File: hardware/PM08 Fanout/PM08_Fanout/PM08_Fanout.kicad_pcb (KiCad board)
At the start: 2 copper layers, 1 part

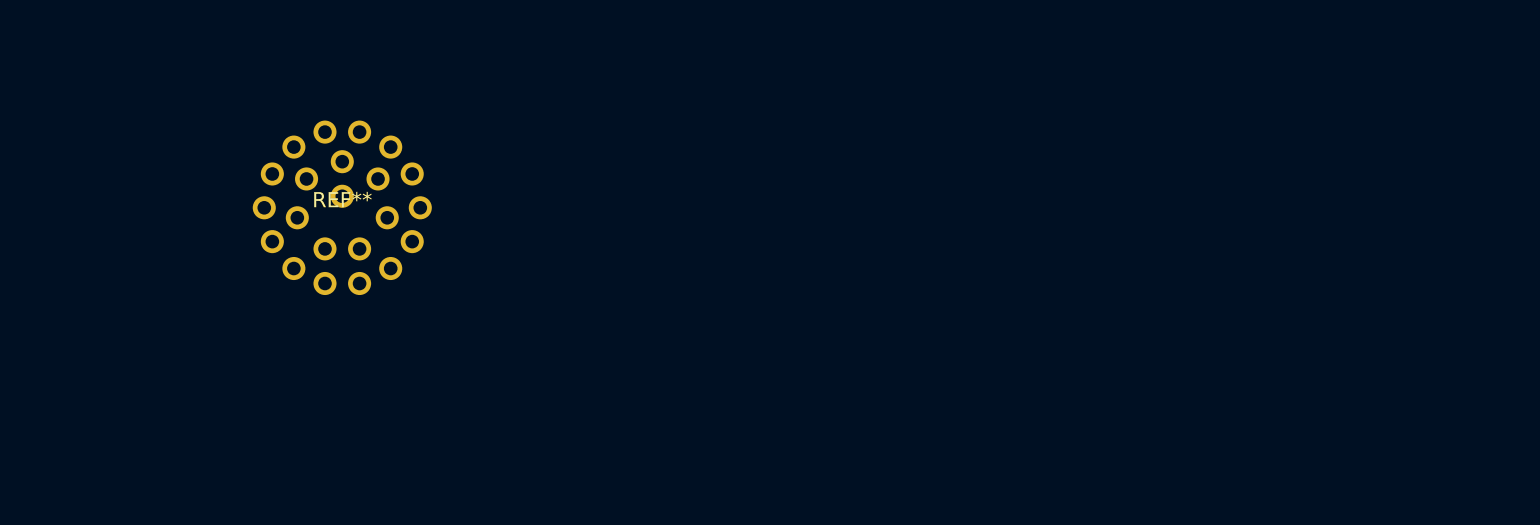
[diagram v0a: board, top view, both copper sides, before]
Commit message: Added PM08 connector board
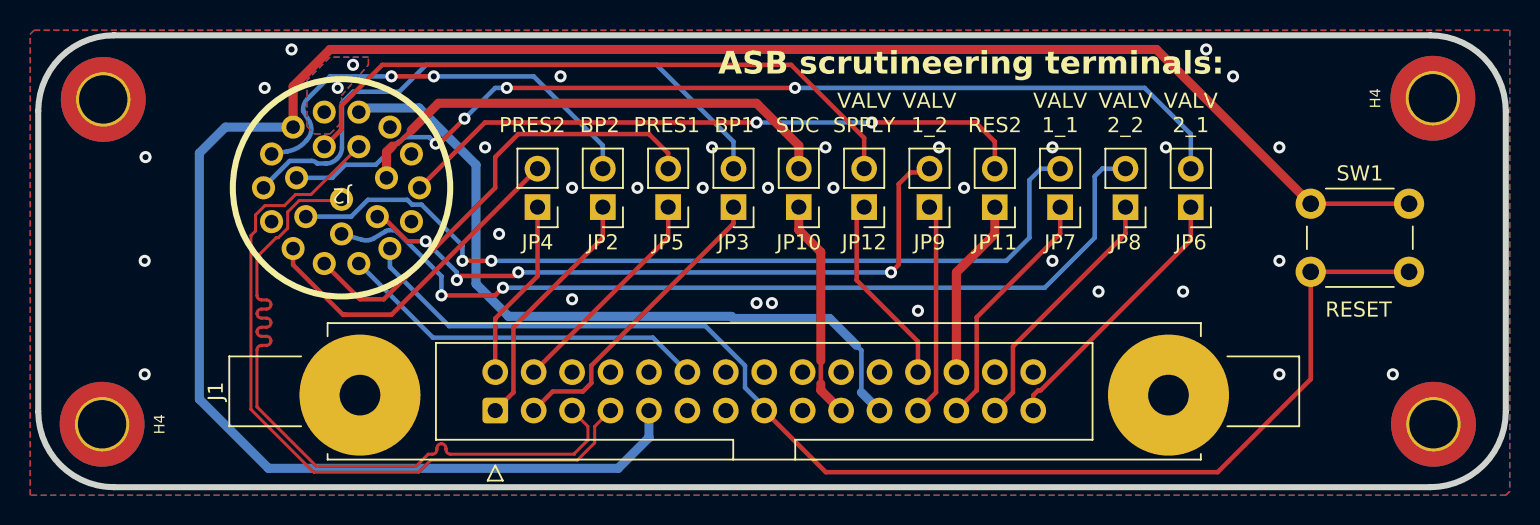
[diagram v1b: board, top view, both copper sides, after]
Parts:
- removed REF**: AS612-35PN, LocalLibrary:AS612-35PN
- added H3: MountingHole_Pad, MountingHole:MountingHole_3.2mm_M3_DIN965_Pad_TopBottom, F.Cu at (201.7, 98.2)
- added H3: MountingHole_Pad, MountingHole:MountingHole_3.2mm_M3_DIN965_Pad_TopBottom, F.Cu at (113.8, 76.7)
- added H4: MountingHole_Pad, MountingHole:MountingHole_3.2mm_M3_DIN965_Pad_TopBottom, F.Cu at (201.7, 76.6)
- added H4: MountingHole_Pad, MountingHole:MountingHole_3.2mm_M3_DIN965_Pad_TopBottom, F.Cu at (113.7, 98.2)
- added J1: IDC Connector, Connector_IDC:IDC-Header_2x15-1MP_P2.54mm_Latch6.5mm_Vertical, F.Cu at (139.7, 97.3)
- added J2: 8STA 22pin, LocalLibrary:AS612-35PN, F.Cu at (129.5, 82.5)
- added JP10: Jumper_2_Open, Connector_PinHeader_2.54mm:PinHeader_1x02_P2.54mm_Vertical, F.Cu at (159.8, 83.8)
- added JP11: Jumper_2_Open, Connector_PinHeader_2.54mm:PinHeader_1x02_P2.54mm_Vertical, F.Cu at (172.7, 83.8)
- added JP12: Jumper_2_Open, Connector_PinHeader_2.54mm:PinHeader_1x02_P2.54mm_Vertical, F.Cu at (164.1, 83.8)
- added JP2: Jumper_2_Open, Connector_PinHeader_2.54mm:PinHeader_1x02_P2.54mm_Vertical, F.Cu at (146.8, 83.8)
- added JP3: Jumper_2_Open, Connector_PinHeader_2.54mm:PinHeader_1x02_P2.54mm_Vertical, F.Cu at (155.4, 83.8)
- added JP4: Jumper_2_Open, Connector_PinHeader_2.54mm:PinHeader_1x02_P2.54mm_Vertical, F.Cu at (142.5, 83.8)
- added JP5: Jumper_2_Open, Connector_PinHeader_2.54mm:PinHeader_1x02_P2.54mm_Vertical, F.Cu at (151.1, 83.8)
- added JP6: Jumper_2_Open, Connector_PinHeader_2.54mm:PinHeader_1x02_P2.54mm_Vertical, F.Cu at (185.7, 83.8)
- added JP7: Jumper_2_Open, Connector_PinHeader_2.54mm:PinHeader_1x02_P2.54mm_Vertical, F.Cu at (177.0, 83.8)
- added JP8: Jumper_2_Open, Connector_PinHeader_2.54mm:PinHeader_1x02_P2.54mm_Vertical, F.Cu at (181.4, 83.8)
- added JP9: Jumper_2_Open, Connector_PinHeader_2.54mm:PinHeader_1x02_P2.54mm_Vertical, F.Cu at (168.4, 83.8)
- added SW1: SW_SPST, Button_Switch_THT:SW_PUSH_6mm, F.Cu at (193.6, 83.6)
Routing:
- net 24v input: track 0.00 -> 139.1 mm
- net EBS_RESET _BUTTON: track 0.00 -> 84.8 mm
- net /solenoid2_I: track 0.00 -> 65.5 mm, vias 0 -> 4
- net /solenoid2_II: track 0.00 -> 60.4 mm, vias 0 -> 2
- net /solenoid1_I: track 0.00 -> 57.3 mm, vias 0 -> 2
- net TSMS: track 0.00 -> 55.7 mm
- net CAN-: track 0.00 -> 49.5 mm
- net SAFETY_OUT: track 0.00 -> 49.1 mm
- net CAN+: track 0.00 -> 49.0 mm
- net /solenoid1_II: track 0.00 -> 44.7 mm, vias 0 -> 4
- net /ASMS: track 0.00 -> 42.1 mm, vias 0 -> 2
- net /BrakePressure1: track 0.00 -> 40.3 mm
- net /SDC_IN: track 0.00 -> 33.5 mm
- net /AirPressure1: track 0.00 -> 31.0 mm
- net /BrakePressure2: track 0.00 -> 29.1 mm, vias 0 -> 2
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- added copper zone on B.Cu, net GND
- added copper zone on F.Cu, net GND
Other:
- board outline added: 97 x 29.9 mm
- board text added: "ASB scrutineering terminals:"
- board text added: "BP1"
- board text added: "BP2"
- board text added: "PRES1"
- board text added: "PRES2"
- board text added: "RES2"
- board text added: "RESET"
- board text added: "SDC"
- board text added: "VALV 1_1"
- board text added: "VALV 1_2"
- board text added: "VALV 2_1"
- board text added: "VALV 2_2"
- board text added: "VALV SPPLY"
- board text added: "{ "ViaStitching": "0.2", "stitch_zone_0": { "HSpacing": "7.5", "VSpacing": "7.5", "Clearance": "0", "Randomize": false } }"
